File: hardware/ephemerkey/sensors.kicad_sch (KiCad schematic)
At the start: 5 parts, among them U5 LIS3DHTR

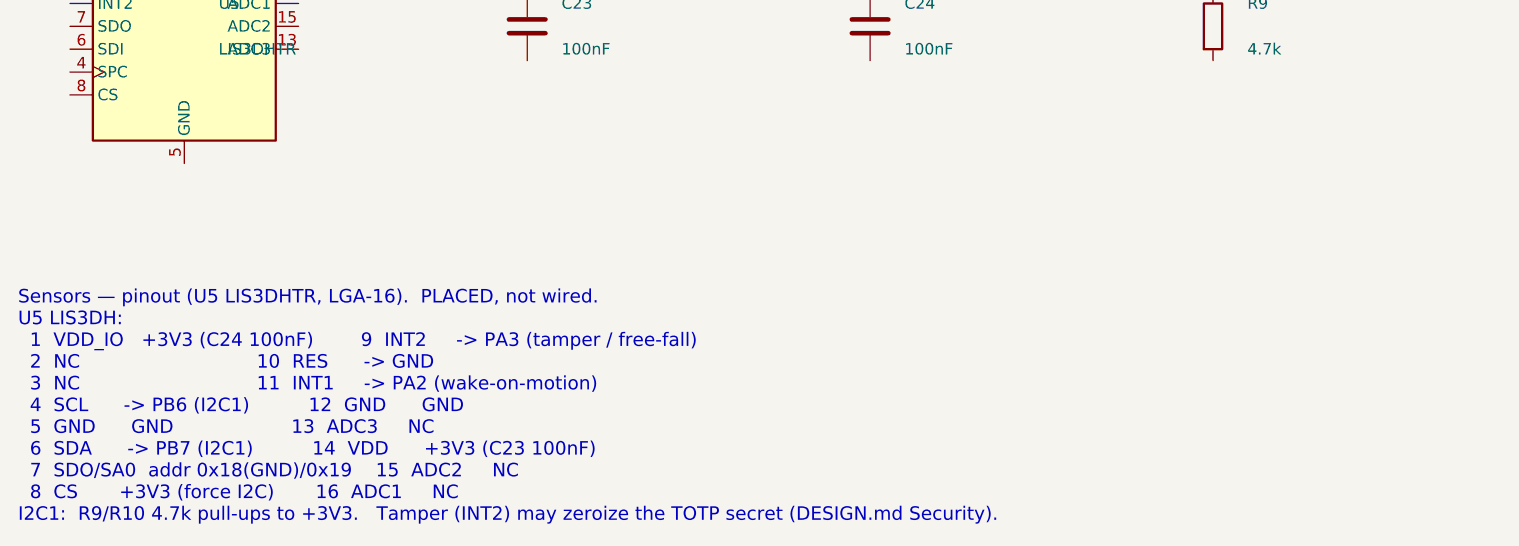
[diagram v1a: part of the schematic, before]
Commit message: lock: second servo output, clearer wiring notes, start PCB layout
- Add a second servo output (J8 + SERVO_SIG2 on PB4, R24/R25) sharing the
  VSERVO rail and the load-switch/interlock -- e.g. a dual-latch lock.
- Rewrite the per-sheet wiring notes (MCU/PWR/DRV) from prose into terse
  pin -> net maps: one line per part, every pin = its net, with a NETS IN
  header for cross-sheet signals. Rationale stays in the README.
- kschgen: park the wiring note below all placed components so the text no
  longer overlaps symbols (computed from the last component row).
- Start the lock PCB layout (hardware/lock/lock.kicad_pcb).

Board regenerates + checks clean (49 components; all footprints carry 3D models).

Co-Authored-By: Claude Opus 4.8 (1M context) <noreply@anthropic.com>
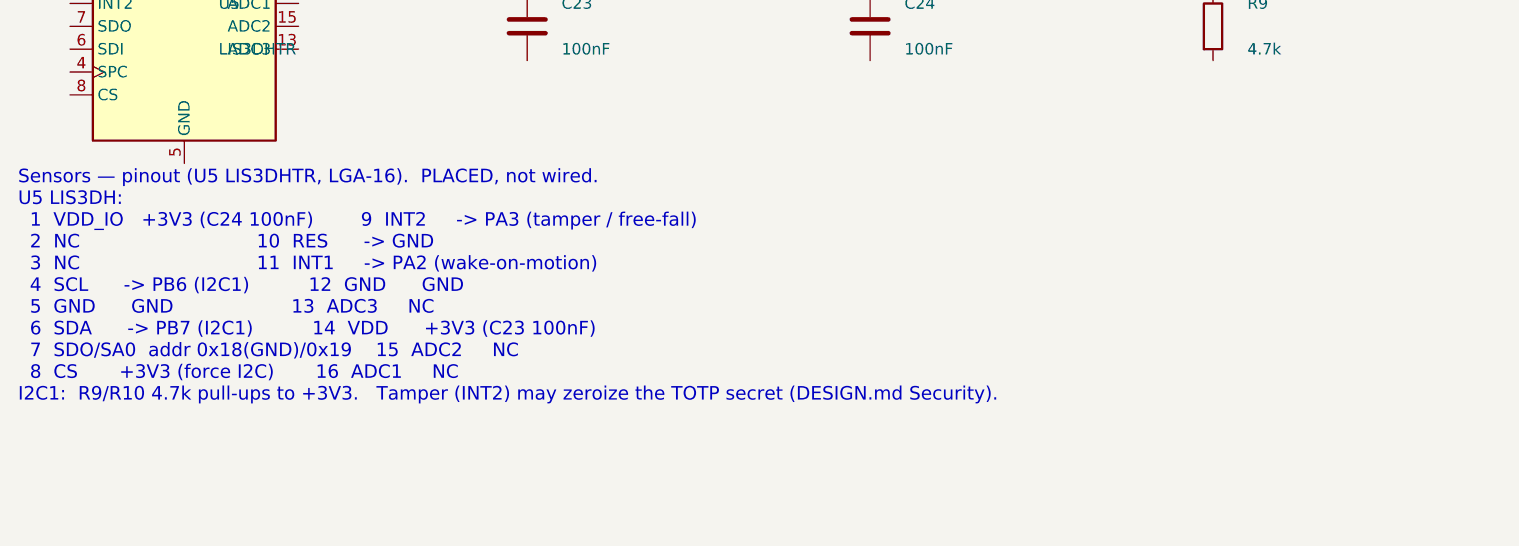
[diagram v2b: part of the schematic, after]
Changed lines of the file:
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@@
 		(instances
 			(project "ephemerkey"
-				(path "/e1000000-0000-4000-8000-000000000001/de451f8d-8860-4120-a9ab-751182c7d03e"
+				(path "/e1000000-0000-4000-8000-000000000001/8103a304-6318-4f63-bdee-ccca8bebf9e9"
 					(reference "U5")
 					(unit 1)
@@
 		(instances
 			(project "ephemerkey"
-				(path "/e1000000-0000-4000-8000-000000000001/de451f8d-8860-4120-a9ab-751182c7d03e"
+				(path "/e1000000-0000-4000-8000-000000000001/8103a304-6318-4f63-bdee-ccca8bebf9e9"
 					(reference "C23")
 					(unit 1)
@@
 		(instances
 			(project "ephemerkey"
-				(path "/e1000000-0000-4000-8000-000000000001/de451f8d-8860-4120-a9ab-751182c7d03e"
+				(path "/e1000000-0000-4000-8000-000000000001/8103a304-6318-4f63-bdee-ccca8bebf9e9"
 					(reference "C24")
 					(unit 1)
@@
 		(instances
 			(project "ephemerkey"
-				(path "/e1000000-0000-4000-8000-000000000001/de451f8d-8860-4120-a9ab-751182c7d03e"
+				(path "/e1000000-0000-4000-8000-000000000001/8103a304-6318-4f63-bdee-ccca8bebf9e9"
 					(reference "R9")
 					(unit 1)
@@
 		(instances
 			(project "ephemerkey"
-				(path "/e1000000-0000-4000-8000-000000000001/de451f8d-8860-4120-a9ab-751182c7d03e"
+				(path "/e1000000-0000-4000-8000-000000000001/8103a304-6318-4f63-bdee-ccca8bebf9e9"
 					(reference "R10")
 					(unit 1)
@@
 	(text "Sensors — pinout (U5 LIS3DHTR, LGA-16).  PLACED, not wired.\nU5 LIS3DH:\n  1  VDD_IO   +3V3 (C24 100nF)        9  INT2     -> PA3 (tamper / free-fall)\n  2  NC                              10  RES      -> GND\n  3  NC                              11  INT1     -> PA2 (wake-on-motion)\n  4  SCL      -> PB6 (I2C1)          12  GND      GND\n  5  GND      GND                    13  ADC3     NC\n  6  SDA      -> PB7 (I2C1)          14  VDD      +3V3 (C23 100nF)\n  7  SDO/SA0  addr 0x18(GND)/0x19    15  ADC2     NC\n  8  CS       +3V3 (force I2C)       16  ADC1     NC\nI2C1:  R9/R10 4.7k pull-ups to +3V3.   Tamper (INT2) may zeroize the TOTP secret (DESIGN.md Security)."
 		(exclude_from_sim no)
-		(at 12.00 70.00 0)
+		(at 12.00 56.64 0)
 		(effects (font (size 1.5 1.5)) (justify left top))
 	)

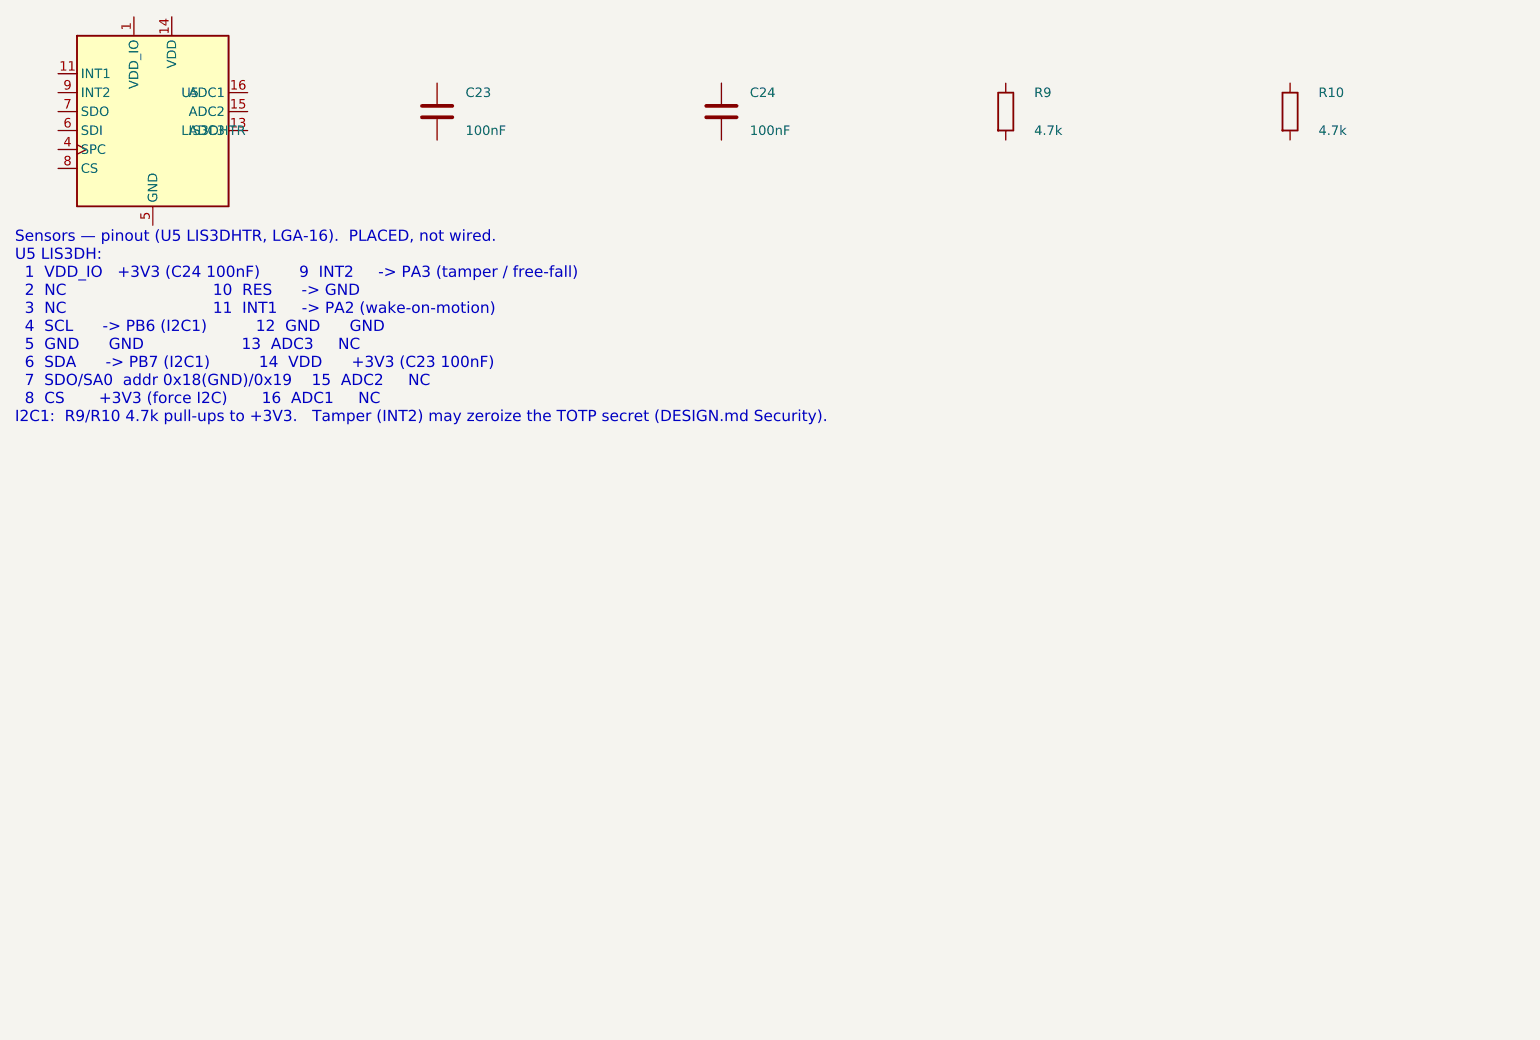
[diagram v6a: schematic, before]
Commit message: hardware: fix PSU load-share S/D, make all sheet notes monospace
The PSU wiring note specified Q1 (AO3401A load-share PMOS) as S=BAT+,
D=VSYS. A PMOS body diode conducts D->S, so that orientation points the
diode VSYS -> BAT+: with USB attached VSYS sits ~4.7V (VBUS - D3) against
a 3.0-4.2V cell, forward-biasing it and dumping uncontrolled current into
the battery, bypassing the MCP73831 charger entirely.

Correct assignment is D=BAT+, S=VSYS, so the body diode points BAT+ ->
VSYS: the battery always reaches the load, and USB can never back-feed
the cell. Q1 was placed but never wired (all three pins are unconnected
in the netlist), so this is a spec fix ahead of wiring, not a board
change. The lock's Q3 is a high-side switch and deliberately uses the
opposite S/D assignment; the note now says so, to stop the two being
"reconciled" by pattern-matching.

Also relaid the PSU note as a two-column table and gave every sheet note
the Courier New face the generator already emits (kschgen NOTE_FONT, added
in 43a6067). The sheets predate that commit, so their notes rendered in
KiCad's variable-width stroke font and the space-padded pin tables did not
line up. Font only on the other six notes -- text is untouched.

Verified: kicad-cli netlists for both boards are byte-identical before and
after (ephemerkey 259 nodes, lock 131 nodes) once the export timestamp is
excluded; no non-font lines changed in any sheet; all sheets re-rendered
and the notes fit inside the page frame.

The four ephemerkey sheets also carry pre-existing eeschema reformatting
(expanded lib_symbols) that was already in the working tree.

Co-Authored-By: Claude Opus 4.8 (1M context) <noreply@anthropic.com>
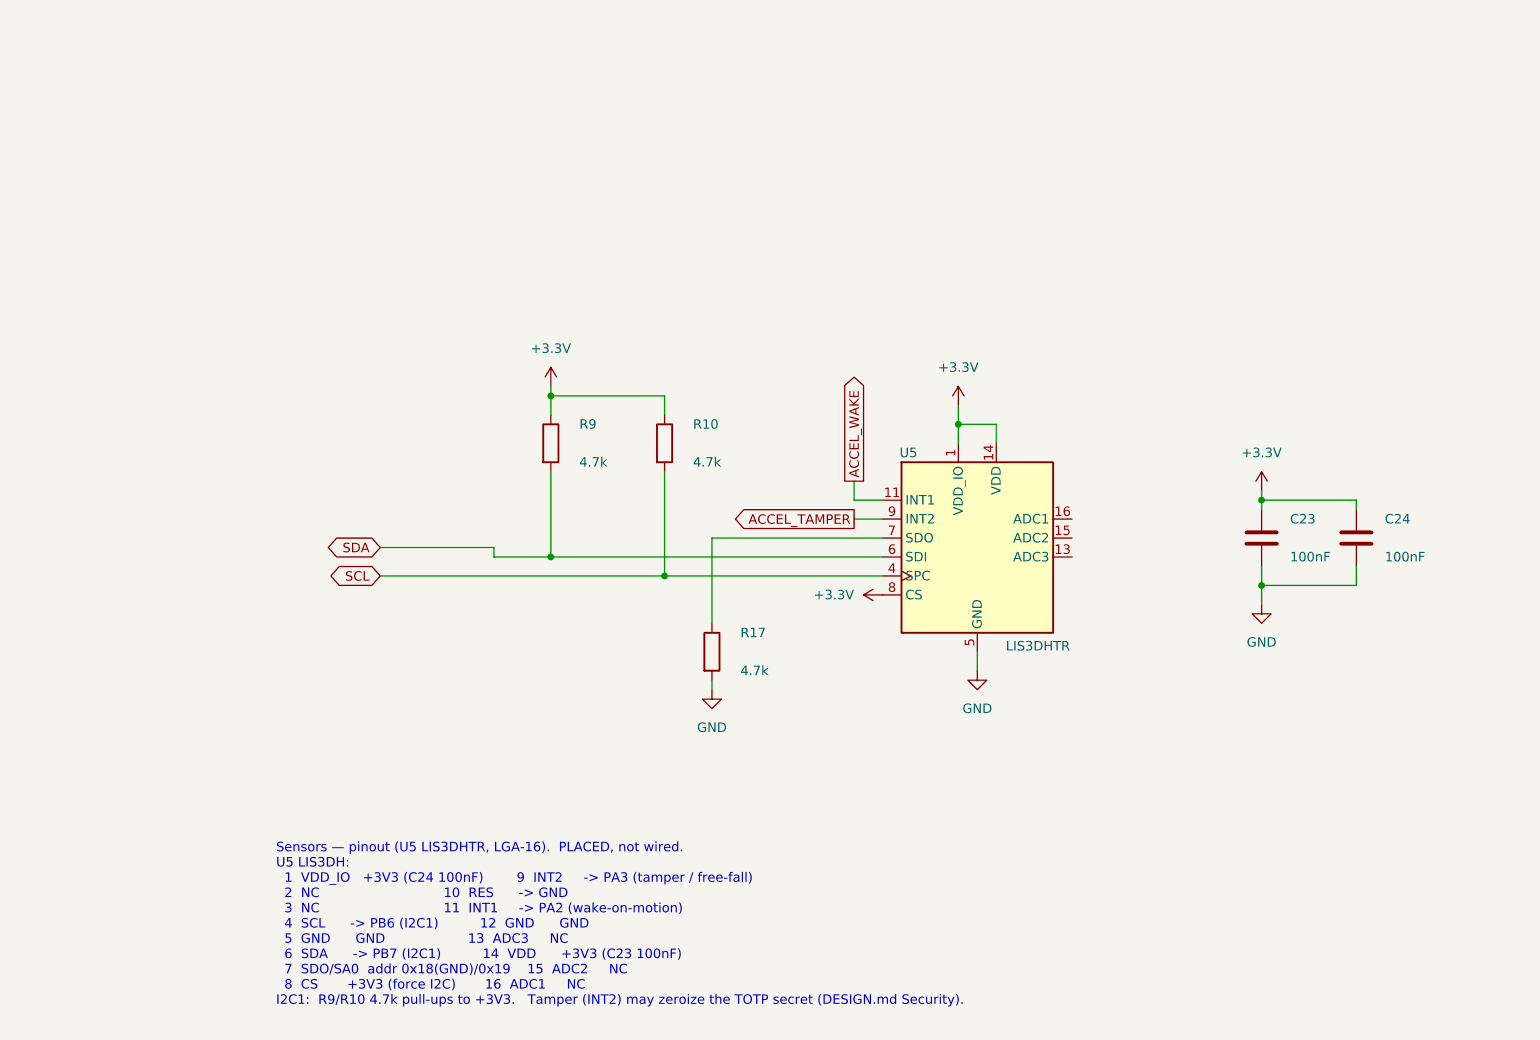
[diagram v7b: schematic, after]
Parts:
- added R17: 4.7k, Resistor_SMD:R_0402_1005Metric, symbol Device:R
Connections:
- net +3.3V: now reaches U5.1 (VDD_IO)
- net +3.3V: now also C23.1, C24.1, R10.1, R9.1, U5.14 (VDD), U5.8 (CS)
- net GND: now reaches U5.10 (GND), U5.12 (GND), U5.5 (GND)
- net GND: now also C23.2, C24.2, R17.2
- net ACCEL_WAKE: now reaches U5.11 (INT1)
- net SCL: now reaches U5.4 (SPC)
- net SCL: now also R10.2
- net SDA: now reaches U5.6 (SDI)
- net SDA: now also R9.2
- net at U5.7 (SDO): now also R17.1
- net ACCEL_TAMPER: now reaches U5.9 (INT2)
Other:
- moved on the sheet: C23, C24, R10, R9, U5

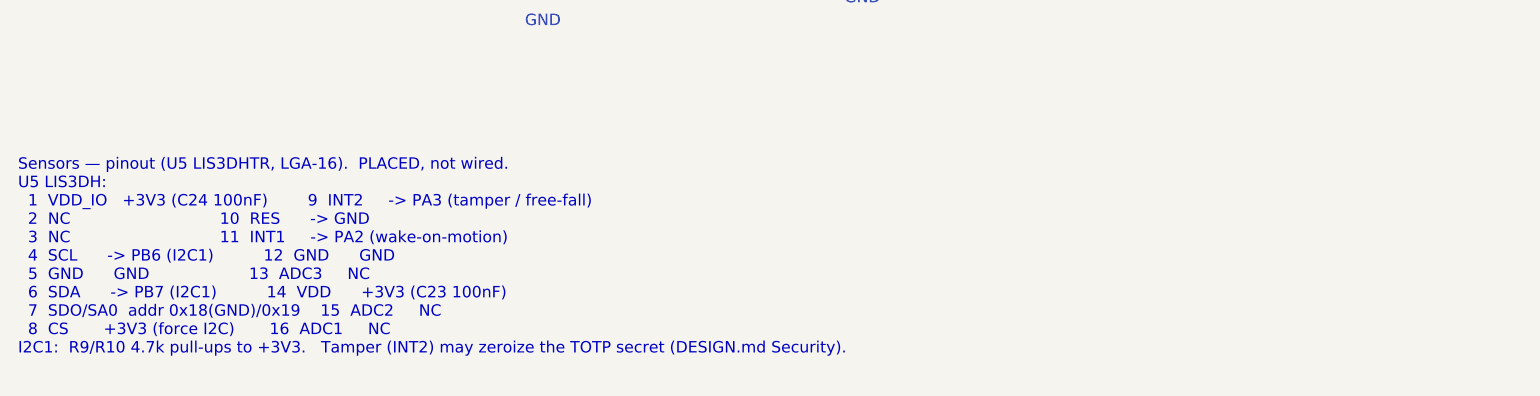
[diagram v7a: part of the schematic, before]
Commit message: hardware+fw: add MAX17048 fuel gauge (U8, I2C1 @0x36) to the PSU sheet
MAX17048G+T10 (LCSC C2682616, TDFN-8 2x2 + EP): 1S ModelGauge SoC monitor,
3uA hibernate, riding the existing I2C1 bus - zero new MCU pins. CELL/VDD
sense at BAT+ (the cell terminal, not VSYS); C31 100nF bypass; CTG/QSTRT/
EP to GND; /ALRT unrouted (no spare pin - firmware polls; alert register
still usable). SDA/SCL logic is independent of VDD, so the 3V3 bus vs a
fading BAT+ is fine.

- Symbol authored into lib/symbols/ephemerkey.kicad_sym from the ADI
  datasheet pin table, cross-checked pin-for-pin against the independently
  authored notchdeck:MAX17048 (sibling project; identical map, same stdlib
  TDFN-8-1EP_2x2mm_P0.5mm_EP0.8x1.2mm footprint). Shared caveat recorded:
  verify EP land vs ADI 21-0168 before fab.
- psu.kicad_sch: surgical splice (sheet is hand-wired; no regen): embedded
  lib symbol, U8 + C31 instances placed near J4, note block updated with
  full pin map + wiring guidance. Property text offsets fixed to be
  relative to the new bodies (KiCad stores them absolute). Render-verified.
- Bus enumerations updated (mcu/sensors/storage notes, manifest + sheets):
  I2C1 = U5 0x18 + DS1 0x3C + U7 0x50-53 + U8 0x36.
- PARTS.md, DESIGN.md (pin table, peripheral summary, BOM).
- ephemerkey-rs: sensors task probes MAX17048 VERSION alongside LIS3DH
  WHO_AM_I; VCELL/SOC register consts staged.

Co-Authored-By: Claude Fable 5 <noreply@anthropic.com>
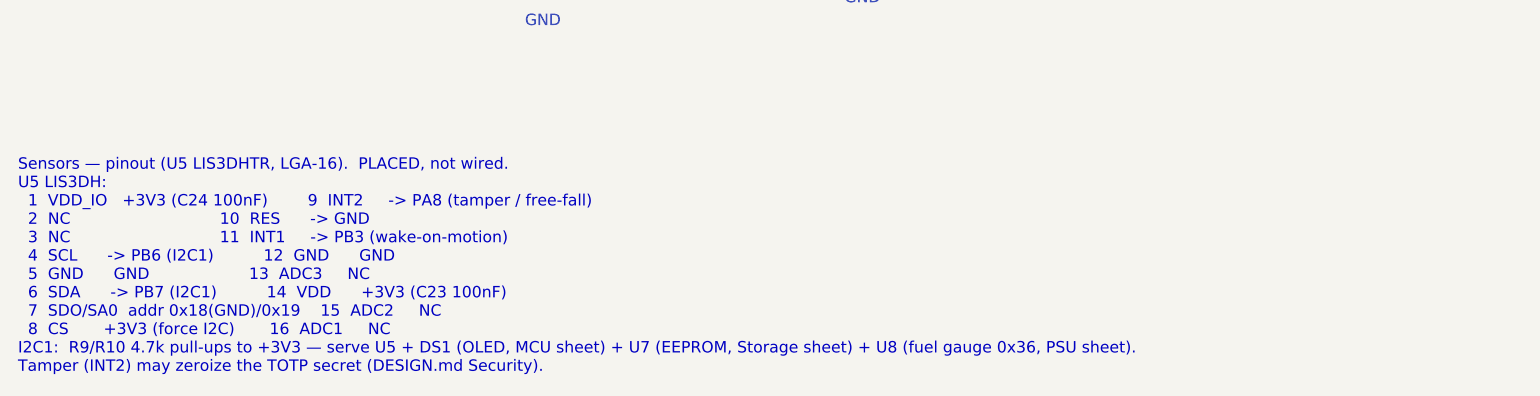
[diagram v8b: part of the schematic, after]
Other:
- note added: "Sensors — pinout (U5 LIS3DHTR, LGA-16). PLACED, not wired. U5 LIS3DH: 1 VDD_IO +3V3 (C24 100nF) 9 INT2 -> PA8 (tamper / free-fall) 2 NC 10 RES -> GND 3 NC 11 INT1 -> PB3 (wake-on-motion) 4 SCL -> PB6 (I2C1) 12 GND GND 5 GND GND 13 ADC3 NC 6 SDA -> PB7 (I2C1) 14 VDD +3V3 (C23 100nF) 7 SDO/SA0 addr 0x18(GND)/0x19 15 ADC2 NC 8 CS +3V3 (force I2C) 16 ADC1 NC I2C1: R9/R10 4.7k pull-ups to +3V3 — serve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"
- note removed: "Sensors — pinout (U5 LIS3DHTR, LGA-16). PLACED, not wired. U5 LIS3DH: 1 VDD_IO +3V3 (C24 100nF) 9 INT2 -> PA3 (tamper / free-fall) 2 NC 10 RES -> GND 3 NC 11 INT1 -> PA2 (wake-on-motion) 4 SCL -> PB6 (I2C1) 12 GND GND 5 GND GND 13 ADC3 NC 6 SDA -> PB7 (I2C1) 14 VDD +3V3 (C23 100nF) 7 SDO/SA0 addr 0x18(GND)/0x19 15 ADC2 NC 8 CS +3V3 (force I2C) 16 ADC1 NC I2C1: R9/R10 4.7k pull-ups to +3V3. Tamper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"
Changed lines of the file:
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@@
 		(company "EphemerKey Authors")
 	)
-	(text "Sensors — pinout (U5 LIS3DHTR, LGA-16).  PLACED, not wired.\nU5 LIS3DH:\n  1  VDD_IO   +3V3 (C24 100nF)        9  INT2     -> PA3 (tamper / free-fall)\n  2  NC                              10  RES      -> GND\n  3  NC                              11  INT1     -> PA2 (wake-on-motion)\n  4  SCL      -> PB6 (I2C1)          12  GND      GND\n  5  GND      GND                    13  ADC3     NC\n  6  SDA      -> PB7 (I2C1)          14  VDD      +3V3 (C23 100nF)\n  7  SDO/SA0  addr 0x18(GND)/0x19    15  ADC2     NC\n  8  CS       +3V3 (force I2C)       16  ADC1     NC\nI2C1:  R9/R10 4.7k pull-ups to +3V3.   Tamper (INT2) may zeroize the TOTP secret (DESIGN.md Security)."
+	(text "Sensors — pinout (U5 LIS3DHTR, LGA-16).  PLACED, not wired.\nU5 LIS3DH:\n  1  VDD_IO   +3V3 (C24 100nF)        9  INT2     -> PA8 (tamper / free-fall)\n  2  NC                              10  RES      -> GND\n  3  NC                              11  INT1     -> PB3 (wake-on-motion)\n  4  SCL      -> PB6 (I2C1)          12  GND      GND\n  5  GND      GND                    13  ADC3     NC\n  6  SDA      -> PB7 (I2C1)          14  VDD      +3V3 (C23 100nF)\n  7  SDO/SA0  addr 0x18(GND)/0x19    15  ADC2     NC\n  8  CS       +3V3 (force I2C)       16  ADC1     NC\nI2C1:  R9/R10 4.7k pull-ups to +3V3 — serve U5 + DS1 (OLED, MCU sheet) + U7 (EEPROM, Storage sheet) + U8 (fuel gauge 0x36, PSU sheet).\nTamper (INT2) may zeroize the TOTP secret (DESIGN.md Security)."
 		(exclude_from_sim no)
 		(at 46.99 138.684 0)
